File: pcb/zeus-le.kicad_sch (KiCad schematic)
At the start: 3 parts

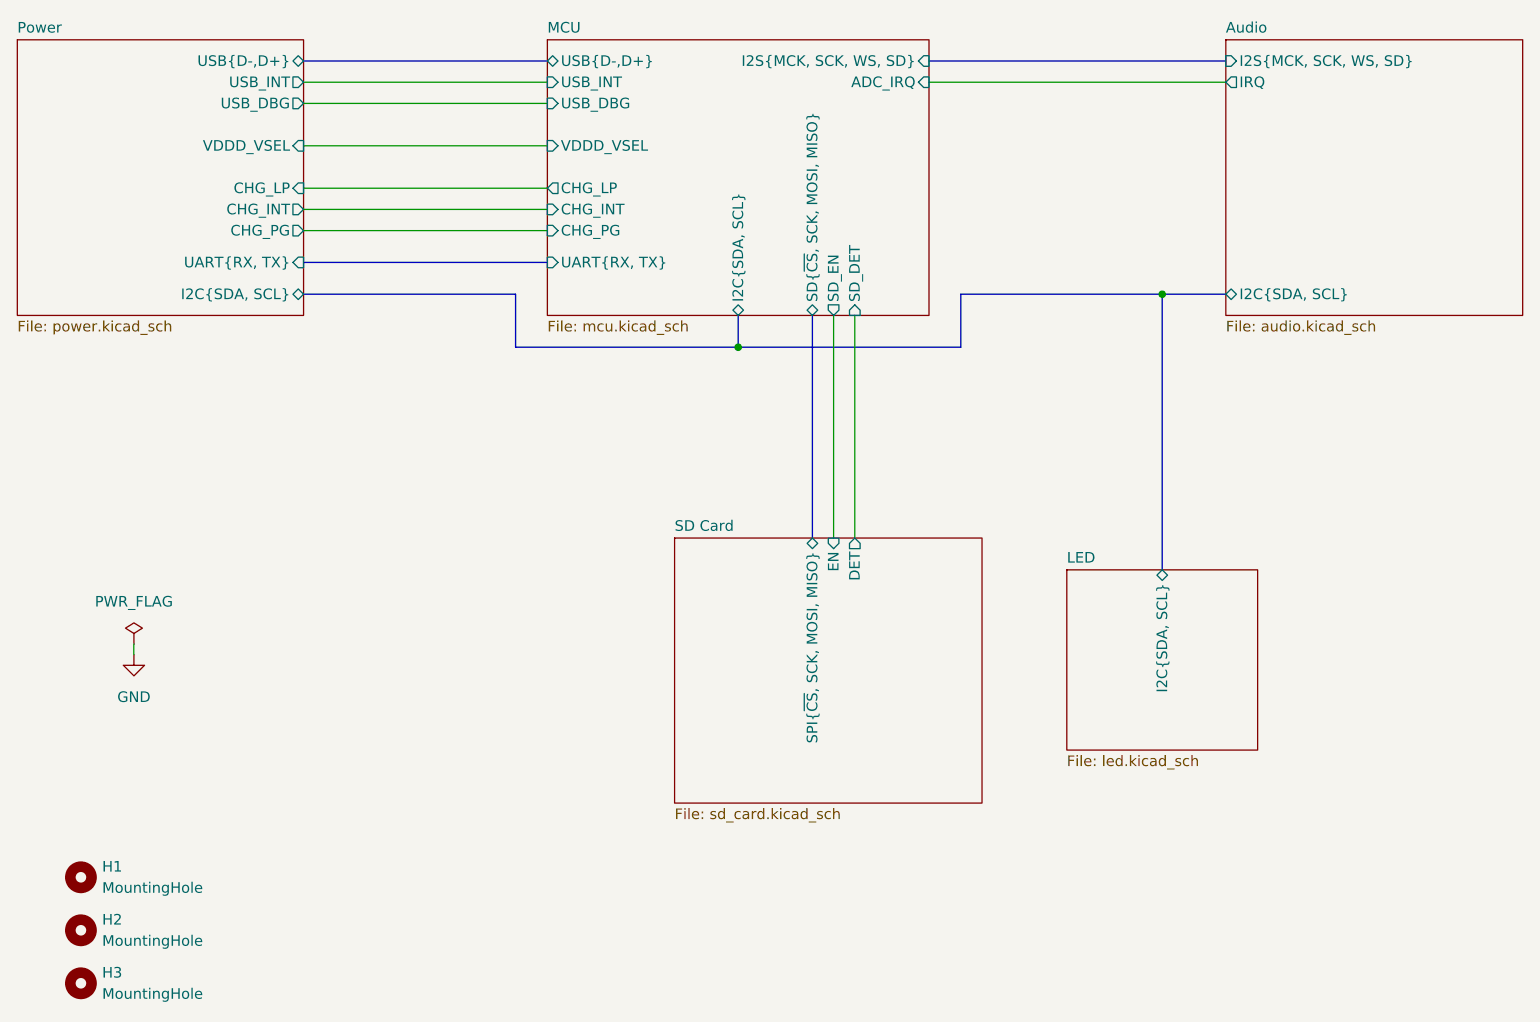
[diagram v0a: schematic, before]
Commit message: pcb: simplify power supply and define LC filter
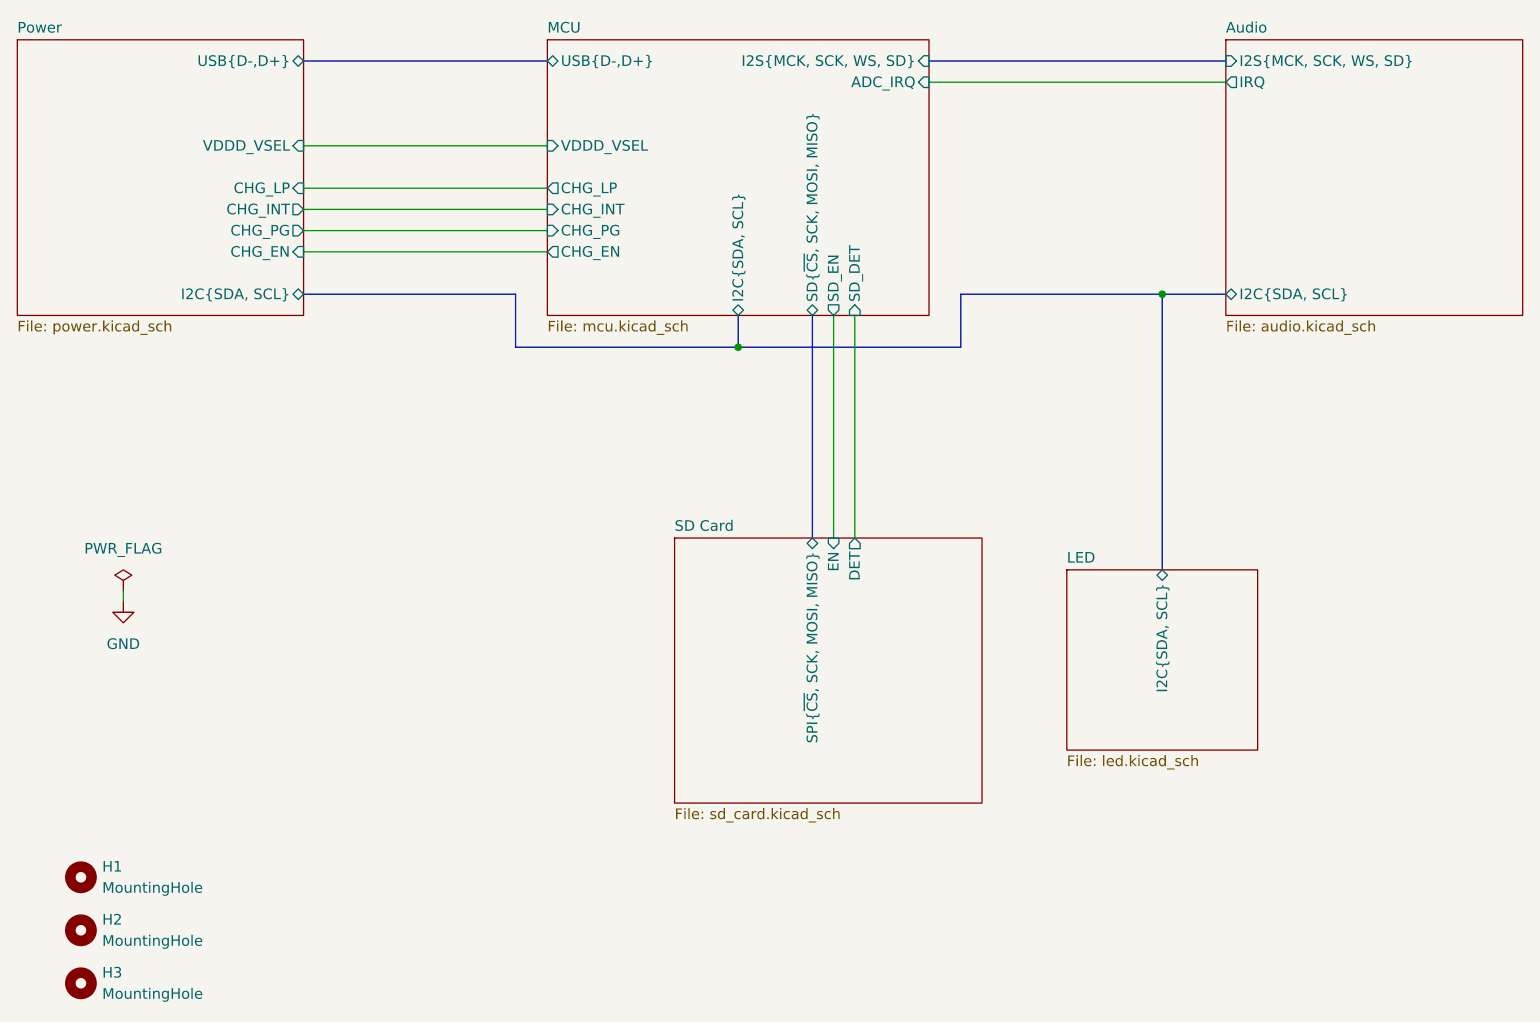
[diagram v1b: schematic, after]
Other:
- sheet MCU ports: added CHG_EN; removed UART{RX, TX}, USB_DBG, USB_INT
- sheet Power ports: added CHG_EN; removed UART{RX, TX}, USB_DBG, USB_INT
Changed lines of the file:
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@@
 		(color 0 0 0 0)
 	)
+	(wire
+		(pts
+			(xy 66.04 116.84) (xy 66.04 115.57)
+		)
+		(stroke
+			(width 0)
+			(type default)
+		)
+	)
 	(bus
 		(pts
@@
 	(wire
 		(pts
+			(xy 87.63 74.93) (xy 116.84 74.93)
+		)
+		(stroke
+			(width 0)
+			(type default)
+		)
+	)
+	(wire
+		(pts
 			(xy 151.13 82.55) (xy 151.13 109.22)
 		)
@@
 		)
 	)
+	(bus
+		(pts
+			(xy 148.59 82.55) (xy 148.59 109.22)
+		)
+		(stroke
+			(width 0)
+			(type default)
+		)
+	)
 	(wire
 		(pts
-			(xy 87.63 54.61) (xy 116.84 54.61)
-		)
-		(stroke
-			(width 0)
-			(type default)
-		)
-	)
-	(bus
-		(pts
-			(xy 148.59 82.55) (xy 148.59 109.22)
+			(xy 87.63 67.31) (xy 116.84 67.31)
 		)
 		(stroke
@@
 	(wire
 		(pts
-			(xy 87.63 67.31) (xy 116.84 67.31)
-		)
-		(stroke
-			(width 0)
-			(type default)
-		)
-	)
-	(bus
-		(pts
-			(xy 87.63 76.2) (xy 116.84 76.2)
-		)
-		(stroke
-			(width 0)
-			(type default)
-		)
-	)
-	(wire
-		(pts
-			(xy 67.31 123.19) (xy 67.31 121.92)
-		)
-		(stroke
-			(width 0)
-			(type default)
-		)
-	)
-	(wire
-		(pts
 			(xy 87.63 72.39) (xy 116.84 72.39)
-		)
-		(stroke
-			(width 0)
-			(type default)
-		)
-	)
-	(wire
-		(pts
-			(xy 87.63 57.15) (xy 116.84 57.15)
 		)
 		(stroke
@@
 	)
 	(symbol
-		(lib_id "power:GND")
-		(at 67.31 123.19 0)
+		(lib_id "power:PWR_FLAG")
+		(at 66.04 115.57 0)
 		(unit 1)
 		(exclude_from_sim no)
@@
 		(dnp no)
 		(fields_autoplaced yes)
-		(property "Reference" "#PWR083"
-			(at 67.31 129.54 0)
-			(effects
-				(font
-					(size 1.27 1.27)
-				)
-				(hide yes)
-			)
-		)
-		(property "Value" "GND"
-			(at 67.31 128.27 0)
+		(property "Reference" "#FLG04"
+			(at 66.04 113.665 0)
+			(effects
+				(font
+					(size 1.27 1.27)
+				)
+				(hide yes)
+			)
+		)
+		(property "Value" "PWR_FLAG"
+			(at 66.04 110.49 0)
 			(effects
 				(font
@@
 		)
 		(property "Footprint" ""
-			(at 67.31 123.19 0)
-			(effects
-				(font
-					(size 1.27 1.27)
-				)
-				(hide yes)
-			)
-		)
-		(property "Datasheet" ""
-			(at 67.31 123.19 0)
-			(effects
-				(font
-					(size 1.27 1.27)
-				)
-				(hide yes)
-			)
-		)
-		(property "Description" "Power symbol creates a global label with name \"GND\" , ground"
-			(at 67.31 123.19 0)
+			(at 66.04 115.57 0)
+			(effects
+				(font
+					(size 1.27 1.27)
+				)
+				(hide yes)
+			)
+		)
+		(property "Datasheet" "~"
+			(at 66.04 115.57 0)
+			(effects
+				(font
+					(size 1.27 1.27)
+				)
+				(hide yes)
+			)
+		)
+		(property "Description" "Special symbol for telling ERC where power comes from"
+			(at 66.04 115.57 0)
 			(effects
 				(font
@@
 			(project "zeus-le"
 				(path "/45d4abf7-8cf8-470c-bd26-f127279c8d1b"
-					(reference "#PWR083")
+					(reference "#FLG04")
+					(unit 1)
+				)
+			)
+		)
+	)
+	(symbol
+		(lib_id "power:GND")
+		(at 66.04 116.84 0)
+		(unit 1)
+		(exclude_from_sim no)
+		(in_bom yes)
+		(on_board yes)
+		(dnp no)
+		(fields_autoplaced yes)
+		(property "Reference" "#PWR016"
+			(at 66.04 123.19 0)
+			(effects
+				(font
+					(size 1.27 1.27)
+				)
+				(hide yes)
+			)
+		)
+		(property "Value" "GND"
+			(at 66.04 121.92 0)
+			(effects
+				(font
+					(size 1.27 1.27)
+				)
+			)
+		)
+		(property "Footprint" ""
+			(at 66.04 116.84 0)
+			(effects
+				(font
+					(size 1.27 1.27)
+				)
+				(hide yes)
+			)
+		)
+		(property "Datasheet" ""
+			(at 66.04 116.84 0)
+			(effects
+				(font
+					(size 1.27 1.27)
+				)
+				(hide yes)
+			)
+		)
+		(property "Description" "Power symbol creates a global label with name \"GND\" , ground"
+			(at 66.04 116.84 0)
+			(effects
+				(font
+					(size 1.27 1.27)
+				)
+				(hide yes)
+			)
+		)
+		(pin "1"
+		)
+		(instances
+			(project "zeus-le"
+				(path "/45d4abf7-8cf8-470c-bd26-f127279c8d1b"
+					(reference "#PWR016")
 					(unit 1)
 				)
@@
 		)
 	)
-	(symbol
-		(lib_id "power:PWR_FLAG")
-		(at 67.31 121.92 0)
-		(unit 1)
-		(exclude_from_sim no)
-		(in_bom yes)
-		(on_board yes)
-		(dnp no)
-		(fields_autoplaced yes)
-		(property "Reference" "#FLG04"
-			(at 67.31 120.015 0)
-			(effects
-				(font
-					(size 1.27 1.27)
-				)
-				(hide yes)
-			)
-		)
-		(property "Value" "PWR_FLAG"
-			(at 67.31 116.84 0)
-			(effects
-				(font
-					(size 1.27 1.27)
-				)
-			)
-		)
-		(property "Footprint" ""
-			(at 67.31 121.92 0)
-			(effects
-				(font
-					(size 1.27 1.27)
-				)
-				(hide yes)
-			)
-		)
-		(property "Datasheet" "~"
-			(at 67.31 121.92 0)
-			(effects
-				(font
-					(size 1.27 1.27)
-				)
-				(hide yes)
-			)
-		)
-		(property "Description" "Special symbol for telling ERC where power comes from"
-			(at 67.31 121.92 0)
-			(effects
-				(font
-					(size 1.27 1.27)
-				)
-				(hide yes)
-			)
-		)
-		(pin "1"
-		)
-		(instances
-			(project "zeus-le"
-				(path "/45d4abf7-8cf8-470c-bd26-f127279c8d1b"
-					(reference "#FLG04")
-					(unit 1)
-				)
-			)
-		)
-	)
 	(sheet
 		(at 53.34 49.53)
@@
 			)
 		)
-		(pin "USB_INT" output
-			(at 87.63 54.61 0)
-			(effects
-				(font
-					(size 1.27 1.27)
-				)
-				(justify right)
-			)
-		)
-		(pin "USB_DBG" output
-			(at 87.63 57.15 0)
-			(effects
-				(font
-					(size 1.27 1.27)
-				)
-				(justify right)
-			)
-		)
 		(pin "CHG_INT" output
 			(at 87.63 69.85 0)
@@
 			)
 		)
-		(pin "UART{RX, TX}" input
-			(at 87.63 76.2 0)
+		(pin "CHG_EN" input
+			(at 87.63 74.93 0)
 			(effects
 				(font
@@
 			)
 		)
-		(pin "USB_DBG" input
-			(at 116.84 57.15 180)
-			(effects
-				(font
-					(size 1.27 1.27)
-				)
-				(justify left)
-			)
-		)
-		(pin "USB_INT" input
-			(at 116.84 54.61 180)
-			(effects
-				(font
-					(size 1.27 1.27)
-				)
-				(justify left)
-			)
-		)
 		(pin "CHG_INT" input
 			(at 116.84 69.85 180)
@@
 			)
 		)
-		(pin "UART{RX, TX}" input
-			(at 116.84 76.2 180)
-			(effects
-				(font
+		(pin "CHG_EN" output
+			(at 116.84 74.93 180)
+			(effects
+				(font
